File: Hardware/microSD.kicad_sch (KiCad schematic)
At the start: 6 parts, among them J3 ST1W008S4TR2000, Q3 DMP3099

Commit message: Finished Boosts and Sensors
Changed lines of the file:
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@@
 (kicad_sch
-	(version 20231120)
+	(version 20250114)
 	(generator "eeschema")
-	(generator_version "8.0")
+	(generator_version "9.0")
 	(paper "A4")
 	(junction
@@
 		(shape input)
 		(at 215.392 77.724 180)
-		(fields_autoplaced yes)
 		(effects
 			(font
@@
 		(shape input)
 		(at 215.392 82.804 180)
-		(fields_autoplaced yes)
 		(effects
 			(font
@@
 		(shape input)
 		(at 214.122 61.468 180)
-		(fields_autoplaced yes)
 		(effects
 			(font
@@
 		(shape output)
 		(at 215.392 87.884 180)
-		(fields_autoplaced yes)
 		(effects
 			(font
@@
 		(shape input)
 		(at 215.392 75.184 180)
-		(fields_autoplaced yes)
 		(effects
 			(font
@@
 		(shape input)
 		(at 210.566 66.294 0)
-		(fields_autoplaced yes)
-		(effects
-			(font
+		(effects
+			(font

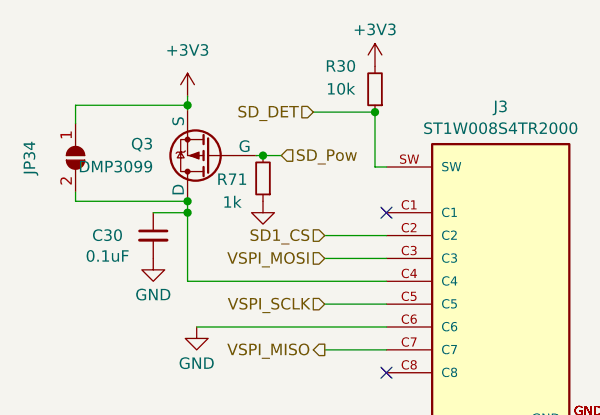
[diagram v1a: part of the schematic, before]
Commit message: Updated SD card, GPIOs, CAN, Power section
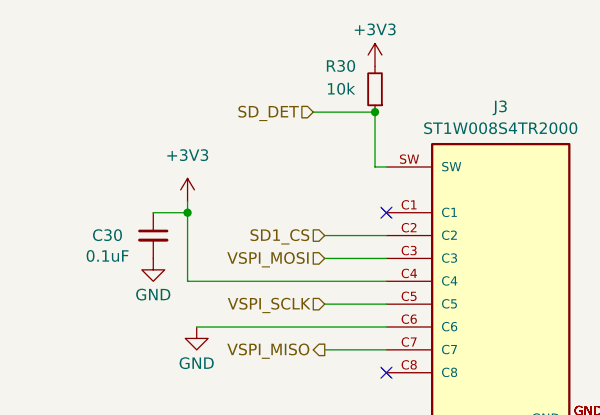
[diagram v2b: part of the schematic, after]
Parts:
- removed JP34: SolderJumper_2_Open, iclr:SmallerSolderJP, symbol Jumper:SolderJumper_2_Open
- removed Q3: DMP3099, Package_TO_SOT_SMD:SOT-23, symbol Simulation_SPICE:PMOS
- removed R71: 1k, Resistor_SMD:R_0402_1005Metric, symbol Device:R_Small
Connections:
- net +3V3: now also C30.1, J3.C4

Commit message: Added actuators and I2C bus
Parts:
- added J16: Conn_01x07_Socket, Connector_Molex:Molex_Pico-Clasp_202396-0707_1x07-1MP_P1.00mm_Horizontal, symbol Connector:Conn_01x07_Socket
- added R13: 10k, Resistor_SMD:R_0402_1005Metric, symbol Device:R_Small
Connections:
- net +3V3: now also J16.7 (Pin_7), R13.1
- net GND: now also J16.4 (Pin_4)
- net VSPI_MISO: now also J16.6 (Pin_6)
- net VSPI_MOSI: now also J16.3 (Pin_3)
- net VSPI_SCLK: now also J16.5 (Pin_5)
- net SD_DET renamed SD1_DET
- new net SD2_CS: J16.2 (Pin_2)
- new net SD2_DET: J16.1 (Pin_1), R13.2

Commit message: schematic reformatting and bom consolidation
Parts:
- C1001: renamed from C30; value 0.1uF -> 100nF
- R1001: renamed from R13; value 10k -> 10kΩ
- R1002: renamed from R30; value 10k -> 10kΩ
- renumbered J16 to J1001, J3 to J1002
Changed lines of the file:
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@@
 		(on_board yes)
 		(dnp no)
-		(property "Reference" "#PWR075"
+		(property "Reference" "#PWR01007"
 			(at 220.98 60.198 0)
 			(effects
@@
 			(project "Ricardo-Stark"
 				(path "/7db990e4-92e1-4f99-b4d2-435bbec1ba83/cbb4aecb-b4d4-4eab-8e16-74accf8129be"
-					(reference "#PWR075")
+					(reference "#PWR01007")
 					(unit 1)
 				)
@@
 		(dnp no)
 		(fields_autoplaced yes)
-		(property "Reference" "R13"
+		(property "Reference" "R1001"
 			(at 131.826 67.5639 0)
 			(effects
@@
 			)
 		)
-		(property "Value" "10k"
+		(property "Value" "10kΩ"
 			(at 131.826 70.1039 0)
 			(effects
@@
 			(project "Ricardo-Stark"
 				(path "/7db990e4-92e1-4f99-b4d2-435bbec1ba83/cbb4aecb-b4d4-4eab-8e16-74accf8129be"
-					(reference "R13")
+					(reference "R1001")
 					(unit 1)
 				)
@@
 		(dnp no)
 		(fields_autoplaced yes)
-		(property "Reference" "J3"
+		(property "Reference" "J1002"
 			(at 234.95 60.8795 0)
 			(effects
@@
 			(project "Ricardo-Stark"
 				(path "/7db990e4-92e1-4f99-b4d2-435bbec1ba83/cbb4aecb-b4d4-4eab-8e16-74accf8129be"
-					(reference "J3")
+					(reference "J1002")
 					(unit 1)
 				)
@@
 		(on_board yes)
 		(dnp no)
-		(property "Reference" "#PWR030"
+		(property "Reference" "#PWR01006"
 			(at 201.168 91.694 0)
 			(effects
@@
 			(project "Ricardo-Stark"
 				(path "/7db990e4-92e1-4f99-b4d2-435bbec1ba83/cbb4aecb-b4d4-4eab-8e16-74accf8129be"
-					(reference "#PWR030")
+					(reference "#PWR01006")
 					(unit 1)
 				)
@@
 		(dnp no)
 		(fields_autoplaced yes)
-		(property "Reference" "#PWR095"
+		(property "Reference" "#PWR01005"
 			(at 200.152 75.184 0)
 			(effects
@@
 			(project "Ricardo-Stark"
 				(path "/7db990e4-92e1-4f99-b4d2-435bbec1ba83/cbb4aecb-b4d4-4eab-8e16-74accf8129be"
-					(reference "#PWR095")
+					(reference "#PWR01005")
 					(unit 1)
 				)
@@
 		(on_board yes)
 		(dnp no)
-		(property "Reference" "#PWR092"
+		(property "Reference" "#PWR01002"
 			(at 125.476 95.504 0)
 			(effects
@@
 			(project "Ricardo-Stark"
 				(path "/7db990e4-92e1-4f99-b4d2-435bbec1ba83/cbb4aecb-b4d4-4eab-8e16-74accf8129be"
-					(reference "#PWR092")
+					(reference "#PWR01002")
 					(unit 1)
 				)
@@
 		(on_board yes)
 		(dnp no)
-		(property "Reference" "R30"
+		(property "Reference" "R1002"
 			(at 217.17 56.388 0)
 			(effects
@@
 			)
 		)
-		(property "Value" "10k"
+		(property "Value" "10kΩ"
 			(at 217.17 58.928 0)
 			(effects
@@
 			(project "Ricardo-Stark"
 				(path "/7db990e4-92e1-4f99-b4d2-435bbec1ba83/cbb4aecb-b4d4-4eab-8e16-74accf8129be"
-					(reference "R30")
+					(reference "R1002")
 					(unit 1)
 				)
@@
 		(dnp no)
 		(fields_autoplaced yes)
-		(property "Reference" "J16"
+		(property "Reference" "J1001"
 			(at 139.446 78.9939 0)
 			(effects
@@
 			(project "Ricardo-Stark"
 				(path "/7db990e4-92e1-4f99-b4d2-435bbec1ba83/cbb4aecb-b4d4-4eab-8e16-74accf8129be"
-					(reference "J16")
+					(reference "J1001")
 					(unit 1)
 				)
@@
 		(on_board yes)
 		(dnp no)
-		(property "Reference" "#PWR094"
+		(property "Reference" "#PWR01004"
 			(at 196.342 84.074 0)
 			(effects
@@
 			(project "Ricardo-Stark"
 				(path "/7db990e4-92e1-4f99-b4d2-435bbec1ba83/cbb4aecb-b4d4-4eab-8e16-74accf8129be"
-					(reference "#PWR094")
+					(reference "#PWR01004")
 					(unit 1)
 				)
@@
 		(dnp no)
 		(fields_autoplaced yes)
-		(property "Reference" "#PWR031"
+		(property "Reference" "#PWR01001"
 			(at 112.776 89.154 0)
 			(effects
@@
 			(project "Ricardo-Stark"
 				(path "/7db990e4-92e1-4f99-b4d2-435bbec1ba83/cbb4aecb-b4d4-4eab-8e16-74accf8129be"
-					(reference "#PWR031")
+					(reference "#PWR01001")
 					(unit 1)
 				)
@@
 		(dnp no)
 		(fields_autoplaced yes)
-		(property "Reference" "#PWR096"
+		(property "Reference" "#PWR01003"
 			(at 129.286 70.104 0)
 			(effects
@@
 			(project "Ricardo-Stark"
 				(path "/7db990e4-92e1-4f99-b4d2-435bbec1ba83/cbb4aecb-b4d4-4eab-8e16-74accf8129be"
-					(reference "#PWR096")
+					(reference "#PWR01003")
 					(unit 1)
 				)
@@
 		(on_board yes)
 		(dnp no)
-		(property "Reference" "C30"
+		(property "Reference" "C1001"
 			(at 191.262 75.184 0)
 			(effects
@@
 			)
 		)
-		(property "Value" "0.1uF"
+		(property "Value" "100nF"
 			(at 191.262 77.4954 0)
 			(effects
@@
 			(project "Ricardo-Stark"
 				(path "/7db990e4-92e1-4f99-b4d2-435bbec1ba83/cbb4aecb-b4d4-4eab-8e16-74accf8129be"
-					(reference "C30")
+					(reference "C1001")
 					(unit 1)
 				)
@@
 		(dnp no)
 		(fields_autoplaced yes)
-		(property "Reference" "#PWR0157"
+		(property "Reference" "#PWR01008"
 			(at 250.19 104.394 0)
 			(effects
@@
 			(project "Ricardo-Stark"
 				(path "/7db990e4-92e1-4f99-b4d2-435bbec1ba83/cbb4aecb-b4d4-4eab-8e16-74accf8129be"
-					(reference "#PWR0157")
-					(unit 1)
-				)
+					(reference "#PWR01008")
+					(unit 1)
+				)
